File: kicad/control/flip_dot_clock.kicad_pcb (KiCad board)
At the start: 4 copper layers, 126.7 x 38.1 mm, 32 parts, among them J1 Conn_01x02_Male, J2 Conn_02x08_Odd_Even, J3 Conn_01x05_Male, U10 Small_7_Seg_FlipDot_Module, U2 SLC03B-05, U3 NCV7719, U4 Small_7_Seg_FlipDot_Module, U5 NCV7719, U6 Small_7_Seg_FlipDot_Module, U7 NCV7719, U8 Small_7_Seg_FlipDot_Module, U9 NCV7719

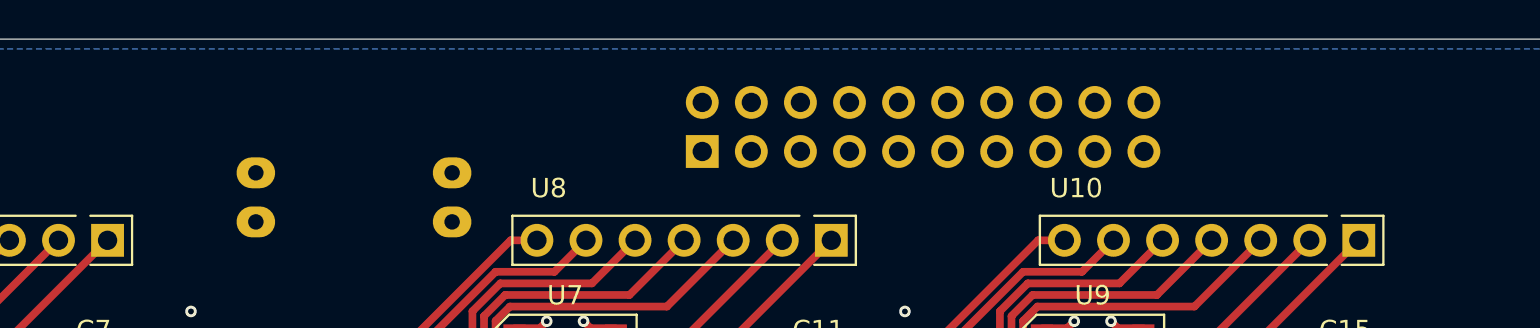
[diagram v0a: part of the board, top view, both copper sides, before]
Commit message: add mounts for nucleo interposer
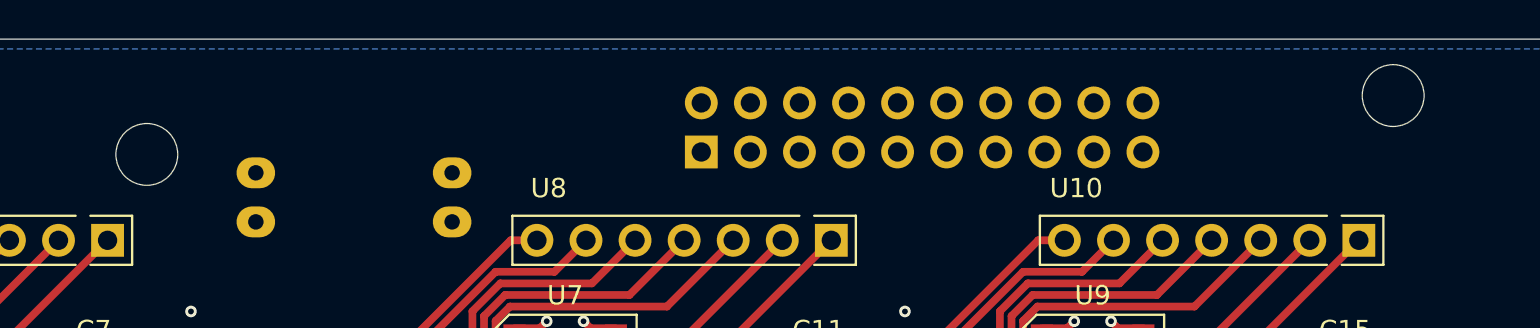
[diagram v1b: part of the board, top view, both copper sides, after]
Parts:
- added REF**: MountingHole_3.2mm_M3, MountingHole:MountingHole_3.2mm_M3, B.Cu at (196.7, 83.3)
- added REF**: MountingHole_3.2mm_M3, MountingHole:MountingHole_3.2mm_M3, B.Cu at (132.2, 86.4)
- moved J2 0.06 mm to (160.9, 86.2)
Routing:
- net /SPI1_MOSI: track 118.0 -> 110.8 mm
- net /SPI1_CS_1: track 86.6 -> 88.4 mm
- net /NCV_EN_1: track 102.2 -> 103.7 mm
- net /MIN_UP: track 60.5 -> 61.6 mm
- net /NCV_EN_2: track 134.0 -> 133.3 mm
- net /HOUR_DOWN: track 52.6 -> 53.2 mm

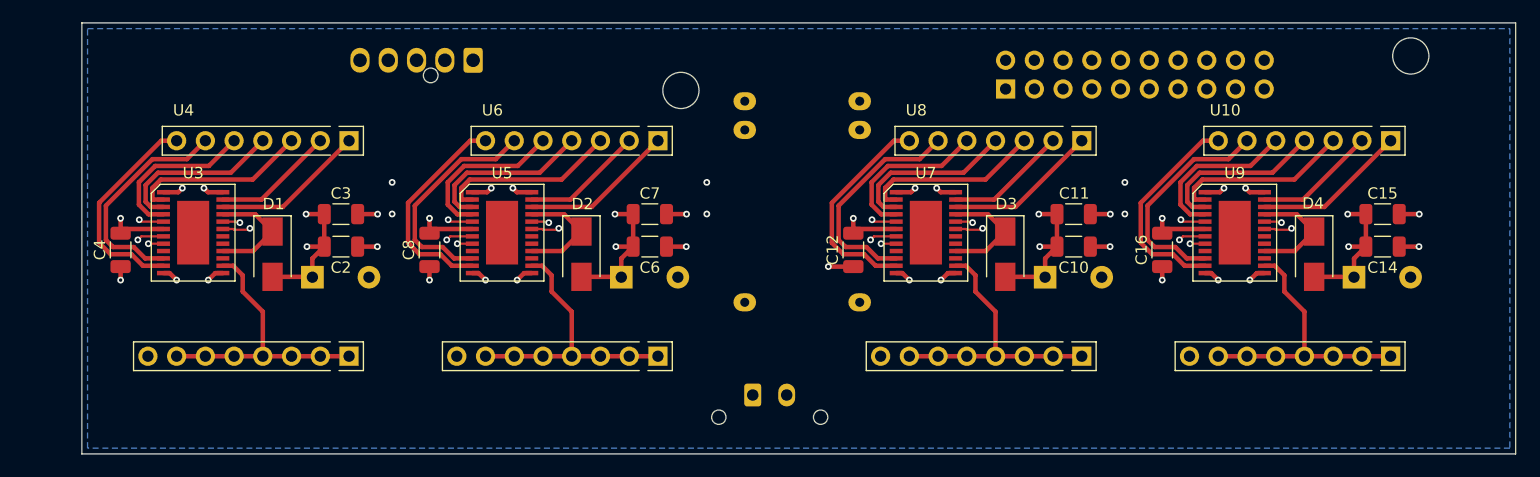
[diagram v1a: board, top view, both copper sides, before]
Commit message: and more ground plane
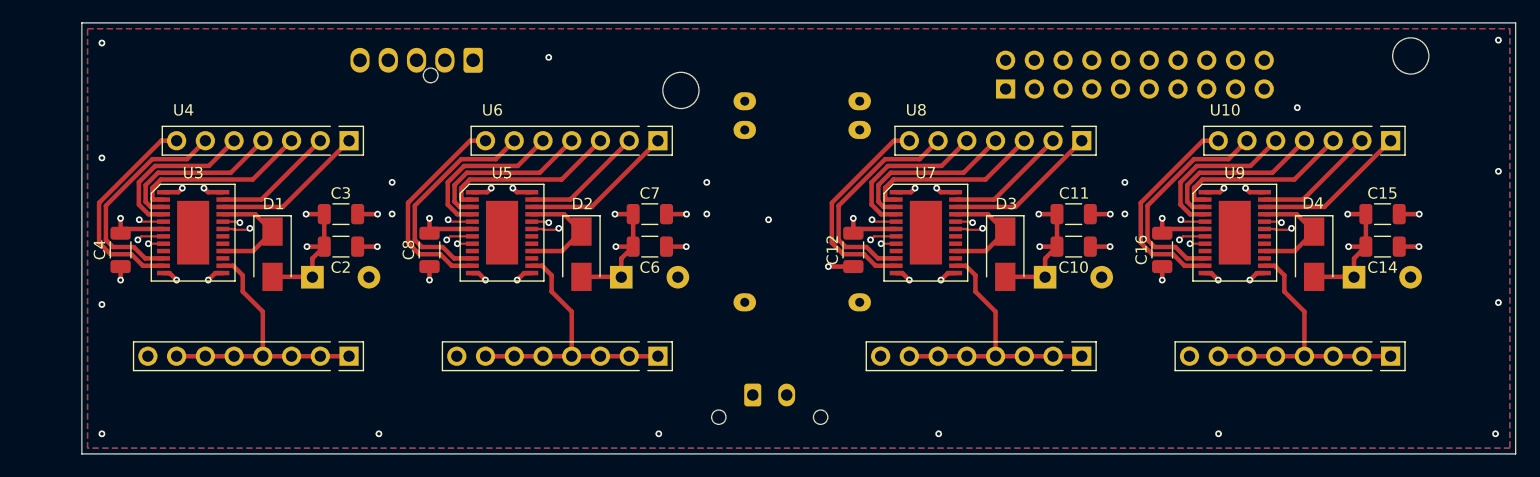
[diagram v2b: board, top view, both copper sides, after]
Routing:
- net GND: vias 28 -> 43
- added copper zone on F.Cu, net GND
- added copper zone on In2.Cu, net GND
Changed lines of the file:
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@@
-(kicad_pcb (version 20220131) (generator pcbnew)
+(kicad_pcb (version 20220211) (generator pcbnew)
   (general
     (thickness 1.756664)
@@
   (segment (start 155.175 95.358) (end 154.813 94.996) (width 0.4) (layer "F.Cu") (net 6))
   (via (at 105.398 97.294) (size 0.6) (drill 0.3) (layers "F.Cu" "B.Cu") (net 6))
+  (via (at 120.523 83.439) (size 0.6) (drill 0.3) (layers "F.Cu" "B.Cu") (free) (net 6))
+  (via (at 81.026 92.329) (size 0.6) (drill 0.3) (layers "F.Cu" "B.Cu") (free) (net 6))
   (via (at 87.63 103.124) (size 0.6) (drill 0.3) (layers "F.Cu" "B.Cu") (net 6))
+  (via (at 81.026 116.713) (size 0.6) (drill 0.3) (layers "F.Cu" "B.Cu") (free) (net 6))
+  (via (at 204.47 93.514333) (size 0.6) (drill 0.3) (layers "F.Cu" "B.Cu") (free) (net 6))
+  (via (at 204.47 105.113666) (size 0.6) (drill 0.3) (layers "F.Cu" "B.Cu") (free) (net 6))
+  (via (at 81.026 82.169) (size 0.6) (drill 0.3) (layers "F.Cu" "B.Cu") (free) (net 6))
   (via (at 82.677 103.124) (size 0.6) (drill 0.3) (layers "F.Cu" "B.Cu") (net 6))
   (via (at 115.443 94.996) (size 0.6) (drill 0.3) (layers "F.Cu" "B.Cu") (net 6))
+  (via (at 105.5116 116.713) (size 0.6) (drill 0.3) (layers "F.Cu" "B.Cu") (free) (net 6))
   (via (at 197.449 100.167) (size 0.6) (drill 0.3) (layers "F.Cu" "B.Cu") (net 6))
+  (via (at 204.216 116.713) (size 0.6) (drill 0.3) (layers "F.Cu" "B.Cu") (free) (net 6))
+  (via (at 139.954 97.79) (size 0.6) (drill 0.3) (layers "F.Cu" "B.Cu") (free) (net 6))
+  (via (at 154.9908 116.713) (size 0.6) (drill 0.3) (layers "F.Cu" "B.Cu") (free) (net 6))
+  (via (at 81.026 105.283) (size 0.6) (drill 0.3) (layers "F.Cu" "B.Cu") (free) (net 6))
   (via (at 152.908 94.996) (size 0.6) (drill 0.3) (layers "F.Cu" "B.Cu") (net 6))
   (via (at 170.144 100.167) (size 0.6) (drill 0.3) (layers "F.Cu" "B.Cu") (net 6))
   (via (at 90.043 94.996) (size 0.6) (drill 0.3) (layers "F.Cu" "B.Cu") (net 6))
+  (via (at 204.47 81.915) (size 0.6) (drill 0.3) (layers "F.Cu" "B.Cu") (free) (net 6))
   (via (at 105.374 100.167) (size 0.6) (drill 0.3) (layers "F.Cu" "B.Cu") (net 6))
   (via (at 117.729 103.124) (size 0.6) (drill 0.3) (layers "F.Cu" "B.Cu") (net 6))
@@
   (via (at 132.703 97.294) (size 0.6) (drill 0.3) (layers "F.Cu" "B.Cu") (net 6))
   (via (at 132.679 100.167) (size 0.6) (drill 0.3) (layers "F.Cu" "B.Cu") (net 6))
+  (via (at 186.69 87.884) (size 0.6) (drill 0.3) (layers "F.Cu" "B.Cu") (free) (net 6))
   (via (at 155.194 103.124) (size 0.6) (drill 0.3) (layers "F.Cu" "B.Cu") (net 6))
   (via (at 152.4 103.124) (size 0.6) (drill 0.3) (layers "F.Cu" "B.Cu") (net 6))
   (via (at 180.213 94.996) (size 0.6) (drill 0.3) (layers "F.Cu" "B.Cu") (net 6))
   (via (at 117.348 94.996) (size 0.6) (drill 0.3) (layers "F.Cu" "B.Cu") (net 6))
+  (via (at 179.7304 116.713) (size 0.6) (drill 0.3) (layers "F.Cu" "B.Cu") (free) (net 6))
   (via (at 114.935 103.124) (size 0.6) (drill 0.3) (layers "F.Cu" "B.Cu") (net 6))
   (via (at 182.499 103.124) (size 0.6) (drill 0.3) (layers "F.Cu" "B.Cu") (net 6))
@@
   (via (at 197.473 97.294) (size 0.6) (drill 0.3) (layers "F.Cu" "B.Cu") (net 6))
   (via (at 88.138 94.996) (size 0.6) (drill 0.3) (layers "F.Cu" "B.Cu") (net 6))
+  (via (at 130.2512 116.713) (size 0.6) (drill 0.3) (layers "F.Cu" "B.Cu") (free) (net 6))
   (segment (start 158.75 98.679) (end 158.877 98.552) (width 0.2) (layer "F.Cu") (net 7))
   (segment (start 157.409 98.608) (end 157.48 98.679) (width 0.2) (layer "F.Cu") (net 7))
@@
   (segment (start 160.8074 81.0514) (end 163.449 83.693) (width 0.2) (layer "In2.Cu") (net 73))
   (segment (start 106.339 83.693) (end 108.9806 81.0514) (width 0.2) (layer "In2.Cu") (net 73))
+  (zone (net 6) (net_name "GND") (layer "F.Cu") (hatch edge 0.508)
+    (connect_pads (clearance 0.508))
+    (min_thickness 0.254) (filled_areas_thickness no)
+    (fill yes (thermal_gap 0.508) (thermal_bridge_width 0.508))
+    (polygon
+      (pts
+        (xy 205.486 117.983)
+        (xy 79.756 117.983)
+        (xy 79.756 80.899)
+        (xy 205.486 80.899)
+      )
+    )
+  )
   (zone (net 5) (net_name "+5V") (layer "In1.Cu") (hatch edge 0.508)
     (connect_pads (clearance 0.508))
@@
       )
     )
+  )
+  (zone (net 6) (net_name "GND") (layer "In2.Cu") (hatch edge 0.508)
+    (connect_pads (clearance 0.3048))
+    (min_thickness 0.254) (filled_areas_thickness no)
+    (fill yes (thermal_gap 0.508) (thermal_bridge_width 0.508))
+    (polygon
+      (pts
+        (xy 205.486 117.983)
+        (xy 79.756 117.983)
+        (xy 79.756 80.899)
+        (xy 205.486 80.899)
+      )
+    )

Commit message: fill zone update
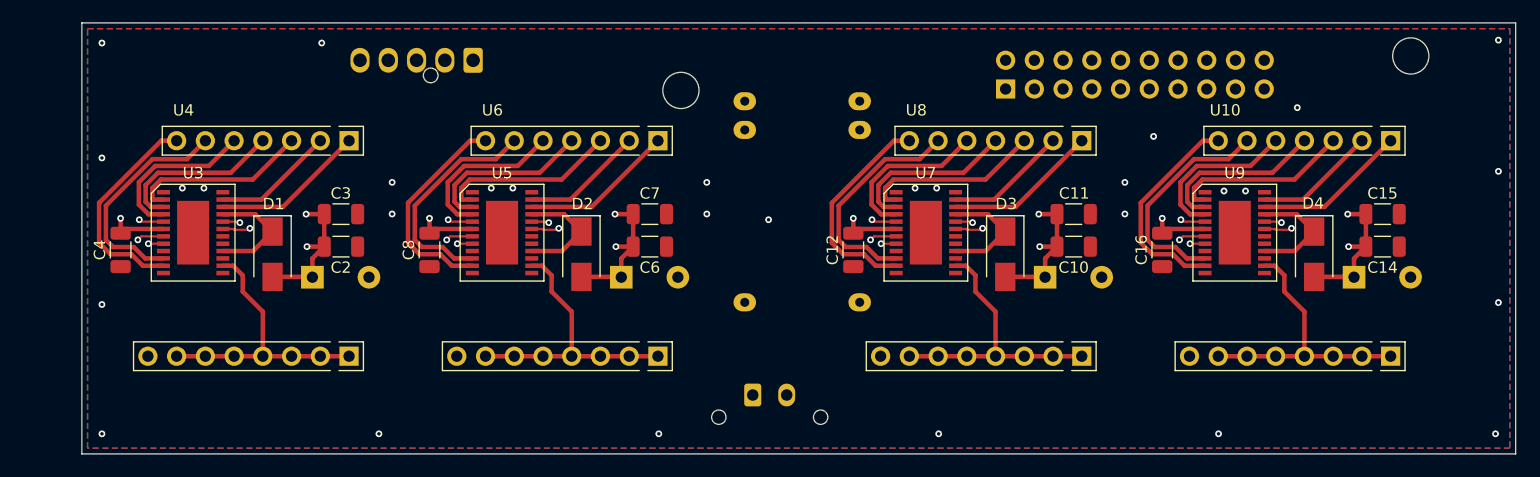
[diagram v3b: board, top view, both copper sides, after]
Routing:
- net GND: track 46.3 -> 0.00 mm, vias 43 -> 24
- net /SPI1_MOSI: track 110.8 -> 118.0 mm

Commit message: add button board. update control ground plane.
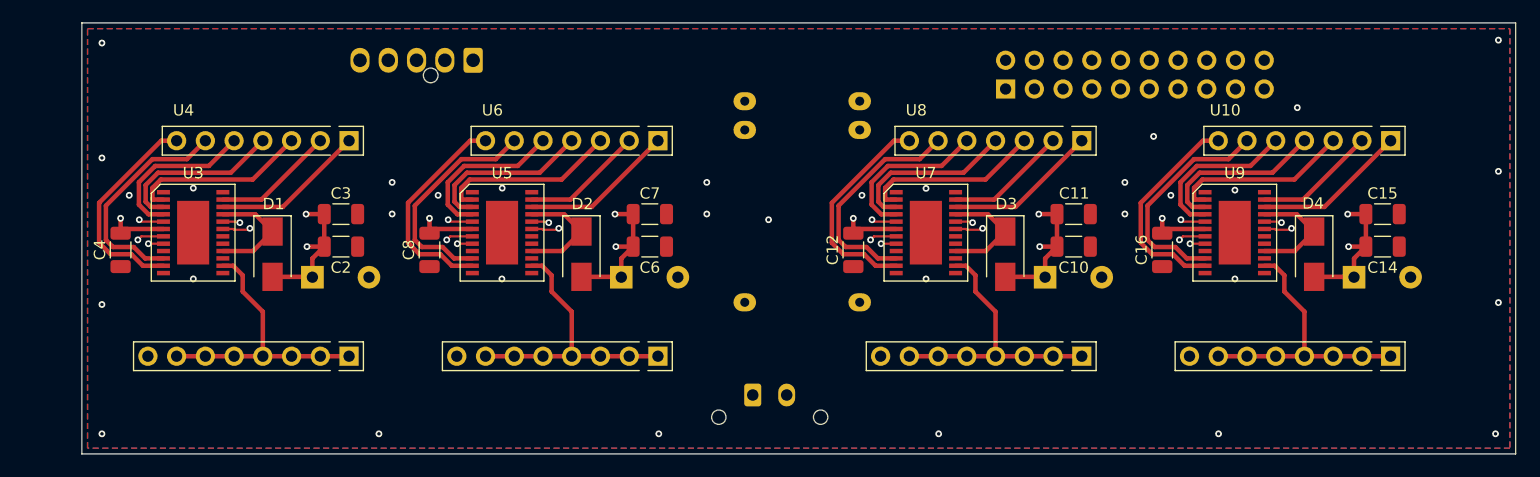
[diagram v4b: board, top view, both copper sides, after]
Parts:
- removed REF** (x2): MountingHole_3.2mm_M3, MountingHole:MountingHole_3.2mm_M3
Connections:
- U3 pad 25: (no net) -> GND
- U5 pad 25: (no net) -> GND
- U7 pad 25: (no net) -> GND
- U9 pad 25: (no net) -> GND
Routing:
- net /NCV_EN_2: track 133.3 -> 134.1 mm
- net GND: vias 24 -> 27

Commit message: update pcb
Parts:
- added H1: MountingHole, mio:MountingHole_3.2mm_M3, B.Cu at (132.2, 86.4)
- added H2: MountingHole, mio:MountingHole_3.2mm_M3, B.Cu at (196.7, 83.3)
- added H3: MountingHole, mio:MountingHole_3.2mm_M3, F.Cu at (77.0, 83.3)
- added H4: MountingHole, mio:MountingHole_3.2mm_M3, F.Cu at (203.2, 83.3)
- added H5: MountingHole, mio:MountingHole_3.2mm_M3, F.Cu at (77.0, 115.6)
- added H6: MountingHole, mio:MountingHole_3.2mm_M3, F.Cu at (203.2, 115.6)
- moved C10 0.13 mm to (167.1, 100.2)
- moved C11 0.13 mm to (167.1, 97.3)
- moved C12 0.13 mm to (147.6, 100.5)
- moved C14 0.13 mm to (194.4, 100.2)
- moved C15 0.13 mm to (194.4, 97.3)
- moved C9 0.13 mm to (164.5, 102.9)
- moved D4 0.13 mm to (188.3, 100.8)
- moved U10 0.13 mm to (173.5, 116.2)
- moved U7 0.13 mm to (154.0, 98.9)
- moved C13 0.13 mm to (191.8, 102.9)
- moved C16 0.13 mm to (174.9, 100.5)
- moved D3 0.13 mm to (161.0, 100.8)
- moved U8 0.13 mm to (146.2, 116.2)
- moved U9 0.13 mm to (181.3, 98.9)
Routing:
- net /HOUR_DOWN: track 53.2 -> 53.9 mm
- net GND: vias 27 -> 26
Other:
- board size 126.7 x 38.1 mm -> 132.1 x 38.1 mm
